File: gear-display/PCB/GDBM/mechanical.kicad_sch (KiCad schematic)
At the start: 7 parts

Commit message: new features
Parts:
- added H? (x5): M2_NPTH_2.2_Minimal, KD_Mechanical_Mounting_Hole:NPTH_3.2mm, symbol KD_Mechanical_Mounting_Hole:NPTH_3.2
- H1: footprint KD_Mechanical_Mounting_Hole:MountingHole_2.2mm_NPTH -> KD_Mechanical_Mounting_Hole:NPTH_3.2mm; symbol KD_Mechanical_Mounting_Hole:M2_NPTH_2.2_Minimal -> KD_Mechanical_Mounting_Hole:NPTH_3.2; Code M2 Mounting Hole -> 3.2 mm hole
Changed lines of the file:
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@@
     (comment 3 "PCB_PN")
   )
+  (symbol (lib_id "KD_Mechanical_Mounting_Hole:NPTH_3.2") (at 63.5 44.45 0) (unit 1)
+    (in_bom yes) (on_board yes) (fields_autoplaced)
+    (property "Reference" "H?" (id 0) (at 66.04 43.1799 0)
+      (effects (font (size 1.27 1.27)) (justify left))
+    )
+    (property "Value" "M2_NPTH_2.2_Minimal" (id 1) (at 50.8 12.7 0)
+      (effects (font (size 1.27 1.27)) (justify left) hide)
+    )
+    (property "Footprint" "KD_Mechanical_Mounting_Hole:NPTH_3.2mm" (id 2) (at 50.8 30.48 0)
+      (effects (font (size 1.27 1.27)) (justify left) hide)
+    )
+    (property "Datasheet" "" (id 3) (at 50.8 33.02 0)
+      (effects (font (size 1.27 1.27)) (justify left) hide)
+    )
+    (property "Code" "3.2 mm hole" (id 4) (at 66.04 45.72 0)
+      (effects (font (size 1.27 1.27)) (justify left))
+    )
+    (property "Manufacturer" "DNP" (id 5) (at 50.8 15.24 0)
+      (effects (font (size 1.27 1.27)) (justify left) hide)
+    )
+    (property "MFG_PartNo" "DNP" (id 6) (at 50.8 17.78 0)
+      (effects (font (size 1.27 1.27)) (justify left) hide)
+    )
+    (property "Supplier" "DNP" (id 7) (at 50.8 20.32 0)
+      (effects (font (size 1.27 1.27)) (justify left) hide)
+    )
+    (property "Supplier_PartNo" "DNP" (id 8) (at 50.8 22.86 0)
+      (effects (font (size 1.27 1.27)) (justify left) hide)
+    )
+    (property "DNP" "T" (id 9) (at 50.8 25.4 0)
+      (effects (font (size 1.27 1.27)) (justify left) hide)
+    )
+    (property "Price" "0.00" (id 10) (at 50.8 27.94 0)
+      (effects (font (size 1.27 1.27)) (justify left) hide)
+    )
+  )
+  (symbol (lib_id "KD_Mechanical_Mounting_Hole:NPTH_3.2") (at 63.5 69.85 0) (unit 1)
+    (in_bom yes) (on_board yes) (fields_autoplaced)
+    (property "Reference" "H?" (id 0) (at 66.04 68.5799 0)
+      (effects (font (size 1.27 1.27)) (justify left))
+    )
+    (property "Value" "M2_NPTH_2.2_Minimal" (id 1) (at 50.8 38.1 0)
+      (effects (font (size 1.27 1.27)) (justify left) hide)
+    )
+    (property "Footprint" "KD_Mechanical_Mounting_Hole:NPTH_3.2mm" (id 2) (at 50.8 55.88 0)
+      (effects (font (size 1.27 1.27)) (justify left) hide)
+    )
+    (property "Datasheet" "" (id 3) (at 50.8 58.42 0)
+      (effects (font (size 1.27 1.27)) (justify left) hide)
+    )
+    (property "Code" "3.2 mm hole" (id 4) (at 66.04 71.12 0)
+      (effects (font (size 1.27 1.27)) (justify left))
+    )
+    (property "Manufacturer" "DNP" (id 5) (at 50.8 40.64 0)
+      (effects (font (size 1.27 1.27)) (justify left) hide)
+    )
+    (property "MFG_PartNo" "DNP" (id 6) (at 50.8 43.18 0)
+      (effects (font (size 1.27 1.27)) (justify left) hide)
+    )
+    (property "Supplier" "DNP" (id 7) (at 50.8 45.72 0)
+      (effects (font (size 1.27 1.27)) (justify left) hide)
+    )
+    (property "Supplier_PartNo" "DNP" (id 8) (at 50.8 48.26 0)
+      (effects (font (size 1.27 1.27)) (justify left) hide)
+    )
+    (property "DNP" "T" (id 9) (at 50.8 50.8 0)
+      (effects (font (size 1.27 1.27)) (justify left) hide)
+    )
+    (property "Price" "0.00" (id 10) (at 50.8 53.34 0)
+      (effects (font (size 1.27 1.27)) (justify left) hide)
+    )
+  )
+  (symbol (lib_id "KD_Mechanical_Mounting_Hole:NPTH_3.2") (at 63.5 57.15 0) (unit 1)
+    (in_bom yes) (on_board yes) (fields_autoplaced)
+    (property "Reference" "H?" (id 0) (at 66.04 55.8799 0)
+      (effects (font (size 1.27 1.27)) (justify left))
+    )
+    (property "Value" "M2_NPTH_2.2_Minimal" (id 1) (at 50.8 25.4 0)
+      (effects (font (size 1.27 1.27)) (justify left) hide)
+    )
+    (property "Footprint" "KD_Mechanical_Mounting_Hole:NPTH_3.2mm" (id 2) (at 50.8 43.18 0)
+      (effects (font (size 1.27 1.27)) (justify left) hide)
+    )
+    (property "Datasheet" "" (id 3) (at 50.8 45.72 0)
+      (effects (font (size 1.27 1.27)) (justify left) hide)
+    )
+    (property "Code" "3.2 mm hole" (id 4) (at 66.04 58.42 0)
+      (effects (font (size 1.27 1.27)) (justify left))
+    )
+    (property "Manufacturer" "DNP" (id 5) (at 50.8 27.94 0)
+      (effects (font (size 1.27 1.27)) (justify left) hide)
+    )
+    (property "MFG_PartNo" "DNP" (id 6) (at 50.8 30.48 0)
+      (effects (font (size 1.27 1.27)) (justify left) hide)
+    )
+    (property "Supplier" "DNP" (id 7) (at 50.8 33.02 0)
+      (effects (font (size 1.27 1.27)) (justify left) hide)
+    )
+    (property "Supplier_PartNo" "DNP" (id 8) (at 50.8 35.56 0)
+      (effects (font (size 1.27 1.27)) (justify left) hide)
+    )
+    (property "DNP" "T" (id 9) (at 50.8 38.1 0)
+      (effects (font (size 1.27 1.27)) (justify left) hide)
+    )
+    (property "Price" "0.00" (id 10) (at 50.8 40.64 0)
+      (effects (font (size 1.27 1.27)) (justify left) hide)
+    )
+  )
   (symbol (lib_id "KD_Mechanical:Fiducial_0.5mm") (at 38.1 44.45 0) (unit 1)
     (in_bom yes) (on_board yes) (fields_autoplaced)
@@
     )
   )
+  (symbol (lib_id "KD_Mechanical_Mounting_Hole:NPTH_3.2") (at 63.5 63.5 0) (unit 1)
+    (in_bom yes) (on_board yes) (fields_autoplaced)
+    (property "Reference" "H?" (id 0) (at 66.04 62.2299 0)
+      (effects (font (size 1.27 1.27)) (justify left))
+    )
+    (property "Value" "M2_NPTH_2.2_Minimal" (id 1) (at 50.8 31.75 0)
+      (effects (font (size 1.27 1.27)) (justify left) hide)
+    )
+    (property "Footprint" "KD_Mechanical_Mounting_Hole:NPTH_3.2mm" (id 2) (at 50.8 49.53 0)
+      (effects (font (size 1.27 1.27)) (justify left) hide)
+    )
+    (property "Datasheet" "" (id 3) (at 50.8 52.07 0)
+      (effects (font (size 1.27 1.27)) (justify left) hide)
+    )
+    (property "Code" "3.2 mm hole" (id 4) (at 66.04 64.77 0)
+      (effects (font (size 1.27 1.27)) (justify left))
+    )
+    (property "Manufacturer" "DNP" (id 5) (at 50.8 34.29 0)
+      (effects (font (size 1.27 1.27)) (justify left) hide)
+    )
+    (property "MFG_PartNo" "DNP" (id 6) (at 50.8 36.83 0)
+      (effects (font (size 1.27 1.27)) (justify left) hide)
+    )
+    (property "Supplier" "DNP" (id 7) (at 50.8 39.37 0)
+      (effects (font (size 1.27 1.27)) (justify left) hide)
+    )
+    (property "Supplier_PartNo" "DNP" (id 8) (at 50.8 41.91 0)
+      (effects (font (size 1.27 1.27)) (justify left) hide)
+    )
+    (property "DNP" "T" (id 9) (at 50.8 44.45 0)
+      (effects (font (size 1.27 1.27)) (justify left) hide)
+    )
+    (property "Price" "0.00" (id 10) (at 50.8 46.99 0)
+      (effects (font (size 1.27 1.27)) (justify left) hide)
+    )
+  )
   (symbol (lib_id "KD_Mechanical:Fiducial_0.5mm") (at 38.1 57.15 0) (unit 1)
     (in_bom yes) (on_board yes) (fields_autoplaced)
@@
     )
   )
+  (symbol (lib_id "KD_Mechanical_Mounting_Hole:NPTH_3.2") (at 63.5 50.8 0) (unit 1)
+    (in_bom yes) (on_board yes) (fields_autoplaced)
+    (property "Reference" "H?" (id 0) (at 66.04 49.5299 0)
+      (effects (font (size 1.27 1.27)) (justify left))
+    )
+    (property "Value" "M2_NPTH_2.2_Minimal" (id 1) (at 50.8 19.05 0)
+      (effects (font (size 1.27 1.27)) (justify left) hide)
+    )
+    (property "Footprint" "KD_Mechanical_Mounting_Hole:NPTH_3.2mm" (id 2) (at 50.8 36.83 0)
+      (effects (font (size 1.27 1.27)) (justify left) hide)
+    )
+    (property "Datasheet" "" (id 3) (at 50.8 39.37 0)
+      (effects (font (size 1.27 1.27)) (justify left) hide)
+    )
+    (property "Code" "3.2 mm hole" (id 4) (at 66.04 52.07 0)
+      (effects (font (size 1.27 1.27)) (justify left))
+    )
+    (property "Manufacturer" "DNP" (id 5) (at 50.8 21.59 0)
+      (effects (font (size 1.27 1.27)) (justify left) hide)
+    )
+    (property "MFG_PartNo" "DNP" (id 6) (at 50.8 24.13 0)
+      (effects (font (size 1.27 1.27)) (justify left) hide)
+    )
+    (property "Supplier" "DNP" (id 7) (at 50.8 26.67 0)
+      (effects (font (size 1.27 1.27)) (justify left) hide)
+    )
+    (property "Supplier_PartNo" "DNP" (id 8) (at 50.8 29.21 0)
+      (effects (font (size 1.27 1.27)) (justify left) hide)
+    )
+    (property "DNP" "T" (id 9) (at 50.8 31.75 0)
+      (effects (font (size 1.27 1.27)) (justify left) hide)
+    )
+    (property "Price" "0.00" (id 10) (at 50.8 34.29 0)
+      (effects (font (size 1.27 1.27)) (justify left) hide)
+    )
+  )
   (symbol (lib_id "KD_Mechanical:Fiducial_0.5mm") (at 38.1 50.8 0) (unit 1)
     (in_bom yes) (on_board yes) (fields_autoplaced)
@@
     )
   )
-  (symbol (lib_id "KD_Mechanical_Mounting_Hole:M2_NPTH_2.2_Minimal") (at 63.5 38.1 0) (unit 1)
+  (symbol (lib_id "KD_Mechanical_Mounting_Hole:NPTH_3.2") (at 63.5 38.1 0) (unit 1)
     (in_bom yes) (on_board yes) (fields_autoplaced)
     (property "Reference" "H1" (id 0) (at 66.04 36.8299 0)
@@
       (effects (font (size 1.27 1.27)) (justify left) hide)
     )
-    (property "Footprint" "KD_Mechanical_Mounting_Hole:MountingHole_2.2mm_NPTH" (id 2) (at 50.8 24.13 0)
+    (property "Footprint" "KD_Mechanical_Mounting_Hole:NPTH_3.2mm" (id 2) (at 50.8 24.13 0)
       (effects (font (size 1.27 1.27)) (justify left) hide)
     )
@@
       (effects (font (size 1.27 1.27)) (justify left) hide)
     )
-    (property "Code" "M2 Mounting Hole" (id 4) (at 66.04 39.3699 0)
-      (effects (font (size 1.27 1.27)) (justify left))
-    )
+    (property "Code" "3.2 mm hole" (id 4) (at 66.04 39.37 0)
+      (effects (font (size 1.27 1.27)) (justify left))
+    )

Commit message: rikki
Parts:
- removed H?: M2_NPTH_2.2_Minimal, KD_Mechanical_Mounting_Hole:NPTH_3.2mm, symbol KD_Mechanical_Mounting_Hole:NPTH_3.2
- added ART1: Artwork_DC_Plug_Polarity, KD_Mechanical:ART_DC_POLARITY, symbol KD_Mechanical:Artwork_DC_Plug_Polarity
- added X?: CON_GND_Probe_Hook, KD_Connector_Pads:GND_HOOK_M, symbol KD_Connector_Pads:CON_GND_Probe_Hook
- FD1, FD2, FD3, FD4, FD5, FD6: now left out of the parts list
- H1: value M2_NPTH_2.2_Minimal -> NPTH_3.2_M3_Clearance; footprint KD_Mechanical_Mounting_Hole:NPTH_3.2mm -> KD_Mechanical_Mounting_Hole:NPTH_3.2mm_M3_clearance; symbol KD_Mechanical_Mounting_Hole:NPTH_3.2 -> KD_Mechanical_Mounting_Hole:NPTH_3.2_M3_Clearance
- H3, H4, H5, H6: renamed from H?; value M2_NPTH_2.2_Minimal -> NPTH_3.2_M3_Clearance; footprint KD_Mechanical_Mounting_Hole:NPTH_3.2mm -> KD_Mechanical_Mounting_Hole:NPTH_3.2mm_M3_clearance; symbol KD_Mechanical_Mounting_Hole:NPTH_3.2 -> KD_Mechanical_Mounting_Hole:NPTH_3.2_M3_Clearance
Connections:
- new net GND: X?.1 (Pin_1), X?.2 (Pin_1)

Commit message: maybe ok
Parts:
- gave numbers to parts that had none: 1
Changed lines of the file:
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@@
   (symbol (lib_id "KD_Connector_Pads:CON_GND_Probe_Hook") (at 124.46 62.23 0) (unit 1)
     (in_bom yes) (on_board yes) (fields_autoplaced)
-    (property "Reference" "X?" (id 0) (at 130.81 61.0638 0)
+    (property "Reference" "X3" (id 0) (at 130.81 61.0638 0)
       (effects (font (size 1.27 1.27)) (justify left))
     )
@@
   (symbol (lib_id "power:GND") (at 127 69.85 0) (unit 1)
     (in_bom yes) (on_board yes) (fields_autoplaced)
-    (property "Reference" "#PWR?" (id 0) (at 127 76.2 0)
+    (property "Reference" "#PWR0143" (id 0) (at 127 76.2 0)
       (effects (font (size 1.27 1.27)) hide)
     )
@@
   (symbol (lib_id "power:GND") (at 119.38 69.85 0) (unit 1)
     (in_bom yes) (on_board yes) (fields_autoplaced)
-    (property "Reference" "#PWR?" (id 0) (at 119.38 76.2 0)
+    (property "Reference" "#PWR0144" (id 0) (at 119.38 76.2 0)
       (effects (font (size 1.27 1.27)) hide)
     )

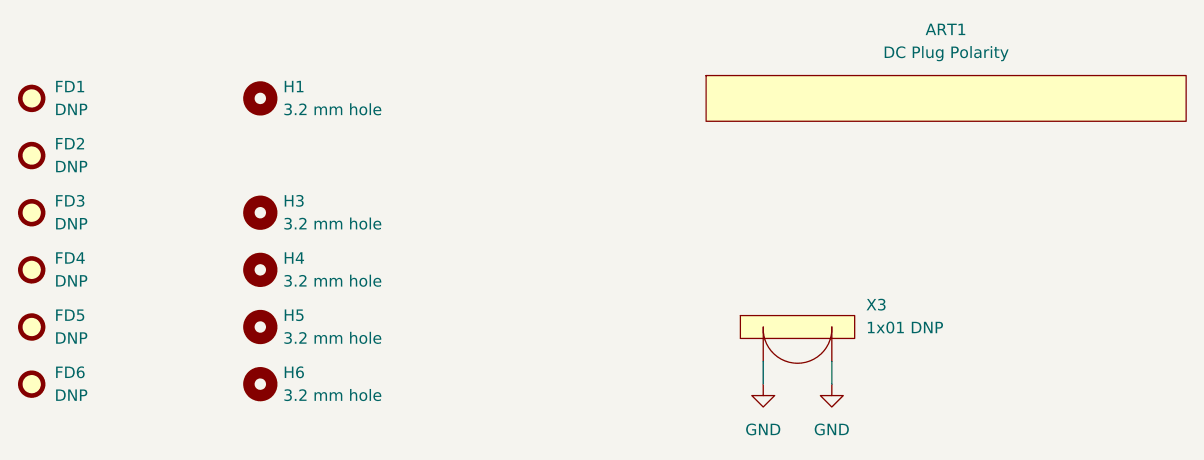
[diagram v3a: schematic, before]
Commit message: bugfixes
added 555 circuit for brightness control
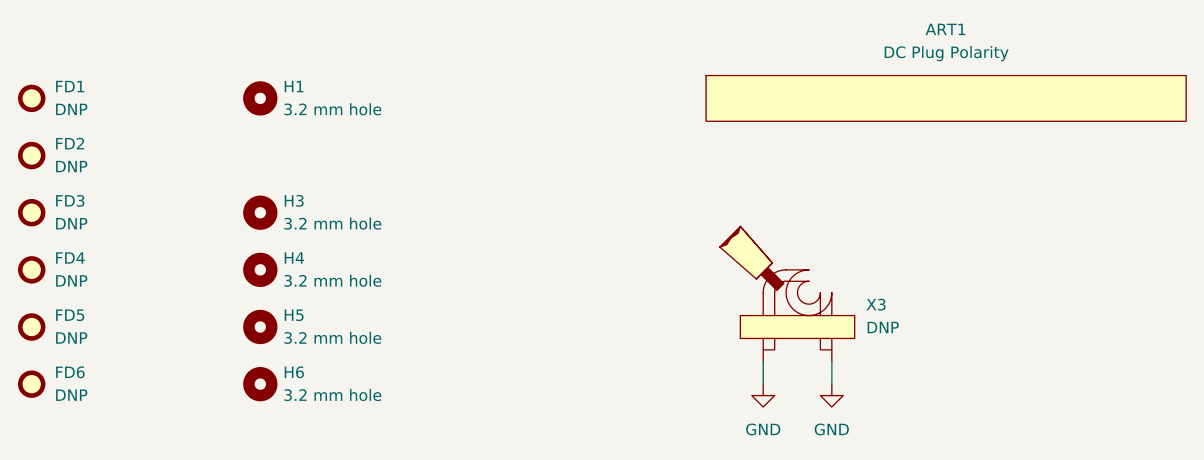
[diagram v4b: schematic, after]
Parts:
- X3: Code 1x01 DNP -> DNP
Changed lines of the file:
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@@
       (effects (font (size 1.27 1.27)) (justify left) hide)
     )
-    (property "Code" "1x01 DNP" (id 4) (at 130.81 63.6038 0)
+    (property "Code" "DNP" (id 4) (at 130.81 63.6038 0)
       (effects (font (size 1.27 1.27)) (justify left))
     )

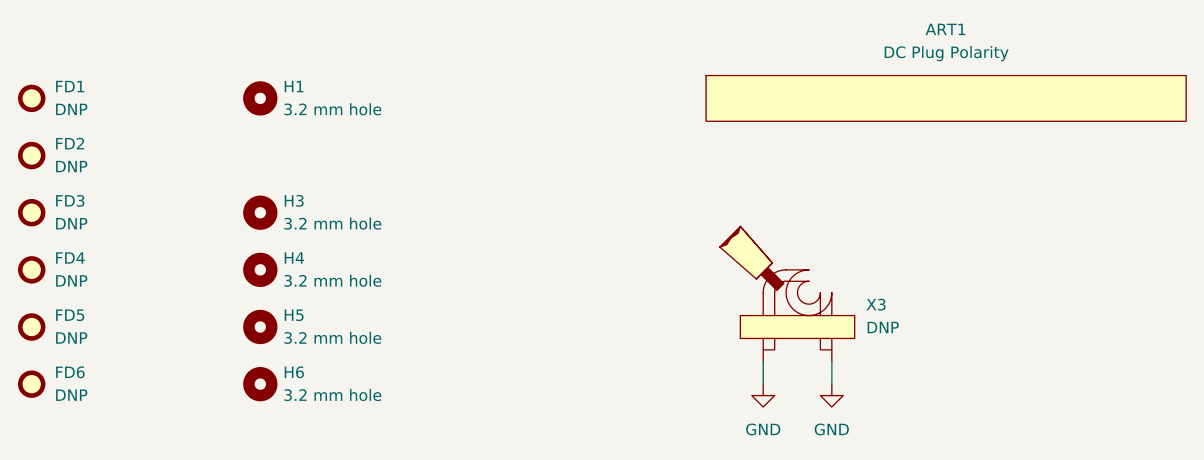
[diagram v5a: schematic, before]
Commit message: change to kicad 7
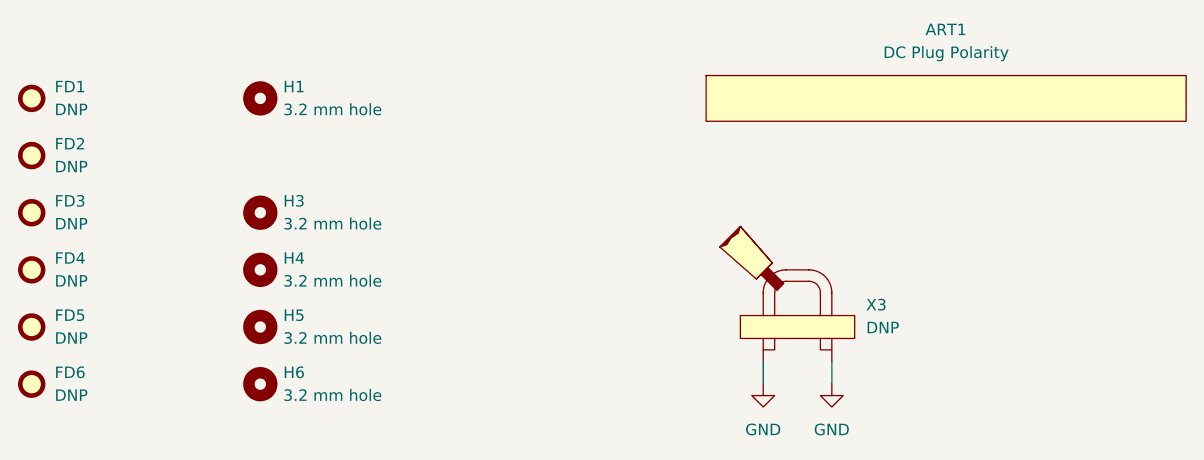
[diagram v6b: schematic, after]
